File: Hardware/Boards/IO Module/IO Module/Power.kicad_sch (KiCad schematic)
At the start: 1 part, among them J1 USB_C_Receptacle

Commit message: Updated IO Module Schematics
Added Power, USB hub and USB-JTAG circuits
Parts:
- added C1, C16, C17, C21, C22, C23, C27, C7, C8, C9: 10uF, Capacitor_SMD:C_0603_1608Metric, symbol Device:C_Small
- added C10, C11, C12, C13, C25, C26: 22uF, Capacitor_SMD:C_0805_2012Metric, symbol Device:C_Small
- added C14, C18, C2, C24: 100nF, Capacitor_SMD:C_0402_1005Metric, symbol Device:C_Small
- added C15, C28: 1uF, Capacitor_SMD:C_0402_1005Metric, symbol Device:C_Small
- added C19, C20: 100uF, Capacitor_SMD:C_0805_2012Metric, symbol Device:C_Small
- added C3, C4: 10nF, Capacitor_SMD:C_0402_1005Metric, symbol Device:C_Small
- added C5, C6: 330pF, Capacitor_SMD:C_0402_1005Metric, symbol Device:C_Small
- added D1: 1V8 FLT, LED_SMD:LED_0603_1608Metric, symbol Device:LED
- added D2: 3V3 FLT, LED_SMD:LED_0603_1608Metric, symbol Device:LED
- added D3: 3V3 ON, LED_SMD:LED_0603_1608Metric, symbol Device:LED
- added D4: 1V8 ON, LED_SMD:LED_0603_1608Metric, symbol Device:LED
- added Q1: IRLML6244, Package_TO_SOT_SMD:SOT-23, symbol Transistor_FET:IRLML6244
- added R1, R14, R15, R16, R2, R24, R26: 3.3K, Resistor_SMD:R_0402_1005Metric, symbol Device:R_US
- added R10: 162K, Resistor_SMD:R_0402_1005Metric, symbol Device:R_US
- added R11: 38K, Resistor_SMD:R_0402_1005Metric, symbol Device:R_US
- added R12: 190K, Resistor_SMD:R_0402_1005Metric, symbol Device:R_US
- added R13: 9.5K, Resistor_SMD:R_0402_1005Metric, symbol Device:R_US
- added R17, R18, R19, R20: 33R, Resistor_SMD:R_0402_1005Metric, symbol Device:R_US
- added R21: 8.06K, Resistor_SMD:R_0402_1005Metric, symbol Device:R_US
- added R22, R28, R3, R4, R5: 10K, Resistor_SMD:R_0402_1005Metric, symbol Device:R_US
- added R23: 26.7K, Resistor_SMD:R_0402_1005Metric, symbol Device:R_US
- added R25: 23.2K, Resistor_SMD:R_0402_1005Metric, symbol Device:R_US
- added R27: 19.8K, Resistor_SMD:R_0402_1005Metric, symbol Device:R_US
- added R29, R30, R31: 1K, Resistor_SMD:R_0402_1005Metric, symbol Device:R_US
- added R6: 198.2K, Resistor_SMD:R_0402_1005Metric, symbol Device:R_US
- added R7: 2.28K, Resistor_SMD:R_0402_1005Metric, symbol Device:R_US
- added R8: 9.4K, Resistor_SMD:R_0402_1005Metric, symbol Device:R_US
- added R9: 191K, Resistor_SMD:R_0402_1005Metric, symbol Device:R_US
- added U1: TPS25730D, IO_Module:TPS25730DREFR, symbol IO_Module:TPS25730D
- added U10: TPD2EUSB30A, Package_TO_SOT_SMD:Texas_DRT-3, symbol Power_Protection:TPD2EUSB30A
- added U11, U9: TPD4EUSB30, Package_SON:USON-10_2.5x1.0mm_P0.5mm, symbol Power_Protection:TPD4EUSB30
- added U2: INA700AYWFR, IO_Module:INA700_AYWFR, symbol IO_Module:INA700
- added U3, U4: TPSM33625RDNR, IO_Module:RDN0011A-MFG, symbol IO_Module:TPSM33625
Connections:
- net GND: now also C1.2, C10.2, C11.2, C12.2, C13.2, C14.2, C15.2, C16.2, C17.2, C18.2, C19.2, C2.2, C20.2, C21.2, C22.2, C23.2, C24.2, C25.2, C26.2, C27.2, C28.2, C3.2, C4.2, C5.2, C6.2, C7.2, C8.2, C9.2, D3.1 (K), Q1.2 (S), R11.1, R13.1, R22.1, R23.1, R27.1, R28.1, R3.1, R31.1, R4.1, R5.1, R7.1, R9.1, U1.11 (GND), U1.12 (GND), U1.14 (GND), U1.16 (GND), U1.17 (GND), U1.31 (GND), U1.34 (GND), U1.35 (GND), U1.39 (EPAD_GND), U10.3 (GND), U11.3 (GND), U11.8 (GND), U2.B1 (GND), U2.B2 (A0), U3.10 (GND), U4.10 (GND), U9.3 (GND), U9.8 (GND)
- net USB3_RX2_N: now reaches J1.A10 (RX2-)
- net USB3_RX2_N: now also U11.2 (D1-), U11.9 (NC)
- net USB3_RX2_P: now reaches J1.A11 (RX2+)
- net USB3_RX2_P: now also U11.1 (D1+), U11.10 (NC)
- net USB3_TX1_P: now reaches J1.A2 (TX1+)
- net USB3_TX1_P: now also U9.4 (D2+), U9.7 (NC)
- net USB3_TX1_N: now reaches J1.A3 (TX1-)
- net USB3_TX1_N: now also U9.5 (D2-), U9.6 (NC)
- net VBUS_IN: now reaches J1.A4 (VBUS), J1.A9 (VBUS), J1.B4 (VBUS), J1.B9 (VBUS)
- net VBUS_IN: now also C1.1, C2.1, C3.1, C4.1, U1.23 (VBUS_IN), U1.24 (VBUS_IN), U1.25 (VBUS_IN), U1.32 (VBUS), U1.33 (VBUS)
- net USB_CC1: now reaches J1.A5 (CC1)
- net USB_CC1: now also C5.1, U1.28 (CC1)
- net USB2_D_P: now reaches J1.A6 (D+)
- net USB2_D_P: now also J1.B6 (D+), U10.1 (D+)
- net USB2_D_N: now reaches J1.A7 (D-)
- net USB2_D_N: now also J1.B7 (D-), U10.2 (D-)
- net USB3_RX1_N: now reaches J1.B10 (RX1-)
- net USB3_RX1_N: now also U9.2 (D1-), U9.9 (NC)
- net USB3_RX1_P: now reaches J1.B11 (RX1+)
- net USB3_RX1_P: now also U9.1 (D1+), U9.10 (NC)
- net USB3_TX2_P: now reaches J1.B2 (TX2+)
- net USB3_TX2_P: now also U11.4 (D2+), U11.7 (NC)
- net USB3_TX2_N: now reaches J1.B3 (TX2-)
- net USB3_TX2_N: now also U11.5 (D2-), U11.6 (NC)
- net USB_CC2: now reaches J1.B5 (CC2)
- net USB_CC2: now also C6.1, U1.29 (CC2)
- new net: R4.2, U1.27 (NC)
- new net: D3.2 (A), R29.2
- new net: D1.1 (K), U3.1 (PGOOD)
- new net: R23.2, U3.11 (RT)
- new net: C15.1, U3.8 (VCC)
- new net: C28.1, U4.8 (VCC)
- new net: D2.1 (K), U4.1 (PGOOD)
- new net: D2.2 (A), R26.2
- new net: D4.1 (K), Q1.3 (D)
- new net: D4.2 (A), R30.1
- new net: R5.2, U1.36 (NC)
- new net: R3.2, U1.26 (NC)
- new net: D1.2 (A), R24.2
- new net: R27.2, U4.11 (RT)
- new net +1V8: C19.1, C20.1, C21.1, Q1.1 (G), R21.2, R31.2, U3.4 (VOUT)
- new net +3V3: C14.1, C25.1, C26.1, C27.1, R14.2, R15.2, R16.2, R25.2, R29.1, R30.2, U2.C1 (VS), U4.4 (VOUT)
- new net I2C0_SCL: R14.1, R17.1, R19.2
- new net I2C0_SDA: R15.1, R18.1, R20.2
- new net I2CT_SCL: R19.1, R2.1, U1.9 (I2CT_SCL)
- new net I2CT_SDA: R1.1, R20.1, U1.8 (I2CT_SDA)
- new net LDO_1V5: C9.1, U1.4 (LDO_1V5)
- new net LDO_3V3: C8.1, R1.2, R10.2, R12.2, R2.2, R24.1, R26.1, R6.2, R8.2, U1.1 (LDO_3V3)
- new net PP1V8_FB: R21.1, R22.2, U3.9 (FB)
- new net PP3V3_FB: R25.1, R28.2, U4.9 (FB)
- new net PP_VUSB: U2.A1 (IN-)
- new net PP_VUSB_R: C10.1, C11.1, C12.1, C13.1, C16.1, C17.1, C18.1, C22.1, C23.1, C24.1, U1.20 (PPHV), U1.21 (PPHV), U1.22 (PPHV), U2.A3 (IN+), U3.2 (EN), U3.3 (VIN), U4.2 (EN), U4.3 (VIN)
- new net USBPD_ADCIN1: R6.1, R7.2, U1.2 (ADCIN1)
- new net USBPD_ADCIN2: R8.1, R9.2, U1.3 (ADCIN2)
- new net USBPD_ADCIN3: R10.1, R11.2, U1.5 (ADCIN3)
- new net USBPD_ADCIN4: R12.1, R13.2, U1.7 (ADCIN4)
- new net USBPD_CAP_MIS: U1.6 (CAP_MIS)
- new net USBPD_DBG_ACC: U1.10 (DBG_ACC)
- new net USBPD_DRAIN: U1.15 (DRAIN), U1.30 (DRAIN), U1.40 (EPAD_DRAIN)
- new net USBPD_FLT_IN: U1.18 (~{FAULT_IN})
- new net USBPD_PLG_EVNT: U1.37 (PLUG_EVENT)
- new net USBPD_PLG_FLIP: U1.13 (PLUG_FLIP)
- new net USBPD_SINK_EN: U1.19 (~{SINK_EN})
- new net VIN_3V3: C7.1, U1.38 (VIN_3V3)
- new net VUSB_ISNS_ALRT: R16.1, U2.C2 (ALRT)
- new net VUSB_ISNS_SCL: R17.2, U2.C3 (SCL)
- new net VUSB_ISNS_SDA: R18.2, U2.B3 (SDA)
- no-connect marks 0 -> 8
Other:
- note added: "1V8 DCDC"
- note added: "3V3 DCDC"
- note added: "ESD DIODES"
- note added: "OUTPUT PORTS"
- note added: "PWR IN + USB-PD CONTROLLER"
- moved on the sheet: J1

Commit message: Completed IO Module Schematics
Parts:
- J1: footprint (none) -> Connector_USB:USB_C_Receptacle_Amphenol_12401548E4-2A
- renumbered C5 to C10, C6 to C11, C7 to C12, C8 to C13, C9 to C14, C22 to C15, C23 to C16, C24 to C17, C25 to C18, C26 to C19, C27 to C20, C28 to C21, C16 to C22, C17 to C23, C18 to C24, C19 to C25, C20 to C26, C21 to C27, C15 to C28, C10 to C5, C11 to C6, C12 to C7, C13 to C8, C14 to C9, D2 to D1, D3 to D2, D4 to D3, D1 to D4, R6 to R10, R8 to R11, R7 to R12, R9 to R13, R10 to R14, R12 to R15, R1 to R16, R2 to R17, R11 to R18, R13 to R19, R3 to R20, R4 to R21, R5 to R22, R26 to R23, R29 to R24, R27 to R26, R28 to R27, R30 to R28, R24 to R29, R17 to R3, R21 to R30, R23 to R32, R22 to R33, R15 to R4, R14 to R5, R16 to R6, R18 to R7, R19 to R8, R20 to R9, U4 to U3, U10 to U4, U9 to U5, U3 to U6, U11 to U7

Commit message: PCB Layout Started
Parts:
- J1: footprint Connector_USB:USB_C_Receptacle_Amphenol_12401548E4-2A -> Connector_USB:USB_C_Receptacle_Amphenol_12401610E4-2A
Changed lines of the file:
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@@
 			)
 		)
-		(property "Footprint" "Connector_USB:USB_C_Receptacle_Amphenol_12401548E4-2A"
+		(property "Footprint" "Connector_USB:USB_C_Receptacle_Amphenol_12401610E4-2A"
 			(at 33.02 49.53 0)
 			(effects

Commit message: Updated SCH with notes & annotations
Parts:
- J1: footprint Connector_USB:USB_C_Receptacle_Amphenol_12401610E4-2A -> IO_Module:GCT_USB4056-03-A_REVA2
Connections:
- net USB3_RX1_N: now also U5.4 (D2+), U5.7 (NC); no longer U5.2 (D1-), U5.9 (NC)
- net USB3_RX1_P: now also U5.5 (D2-), U5.6 (NC); no longer U5.1 (D1+), U5.10 (NC)
- net USB3_TX1_N: now also U5.1 (D1+), U5.10 (NC); no longer U5.5 (D2-), U5.6 (NC)
- net USB3_TX1_P: now also U5.2 (D1-), U5.9 (NC); no longer U5.4 (D2+), U5.7 (NC)

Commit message: Updated PCB routing for IO Module
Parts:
- C10, C11, C17, C2, C21, C24, C28, C3, C4, C9: footprint Capacitor_SMD:C_0402_1005Metric -> Capacitor_SMD:C_0201_0603Metric
- R10, R11, R12, R13, R14, R15, R18, R19, R20, R21, R22, R23, R24, R25, R26, R27, R28, R29, R3, R30, R31, R32, R33, R4, R5, R6, R7, R8, R9: footprint Resistor_SMD:R_0402_1005Metric -> Resistor_SMD:R_0201_0603Metric
- R16, R17: footprint Resistor_SMD:R_0402_1005Metric -> Resistor_SMD:R_0201_0603Metric; now fitted
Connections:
- net USB3_RX1_N: now also J1.B11 (RX1+), U5.5 (D2-), U5.6 (NC); no longer J1.B10 (RX1-), U5.4 (D2+), U5.7 (NC)
- net USB3_RX1_P: now also J1.B10 (RX1-), U5.4 (D2+), U5.7 (NC); no longer J1.B11 (RX1+), U5.5 (D2-), U5.6 (NC)
- net USB3_RX2_N: now also U7.5 (D2-), U7.6 (NC); no longer U7.2 (D1-), U7.9 (NC)
- net USB3_RX2_P: now also U7.4 (D2+), U7.7 (NC); no longer U7.1 (D1+), U7.10 (NC)
- net USB3_TX2_N: now also U7.2 (D1-), U7.9 (NC); no longer U7.5 (D2-), U7.6 (NC)
- net USB3_TX2_P: now also U7.1 (D1+), U7.10 (NC); no longer U7.4 (D2+), U7.7 (NC)

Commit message: Cleaned up routing for IO module
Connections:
- net USB3_TX1_N: now also J1.A2 (TX1+), U5.2 (D1-), U5.9 (NC); no longer J1.A3 (TX1-), U5.1 (D1+), U5.10 (NC)
- net USB3_TX1_P: now also J1.A3 (TX1-), U5.1 (D1+), U5.10 (NC); no longer J1.A2 (TX1+), U5.2 (D1-), U5.9 (NC)
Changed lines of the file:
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@@
 	(wire
 		(pts
-			(xy 226.06 214.63) (xy 212.09 214.63)
-		)
-		(stroke
-			(width 0)
-			(type default)
-		)
-	)
-	(wire
-		(pts
 			(xy 107.95 118.11) (xy 121.92 118.11)
 		)
@@
 	(wire
 		(pts
+			(xy 226.06 224.79) (xy 212.09 224.79)
+		)
+		(stroke
+			(width 0)
+			(type default)
+		)
+	)
+	(wire
+		(pts
 			(xy 106.68 252.73) (xy 120.65 252.73)
 		)
@@
 	(wire
 		(pts
-			(xy 226.06 229.87) (xy 212.09 229.87)
-		)
-		(stroke
-			(width 0)
-			(type default)
-		)
-	)
-	(wire
-		(pts
 			(xy 69.85 83.82) (xy 69.85 82.55)
 		)
@@
 	(wire
 		(pts
+			(xy 226.06 214.63) (xy 212.09 214.63)
+		)
+		(stroke
+			(width 0)
+			(type default)
+		)
+	)
+	(wire
+		(pts
 			(xy 99.06 73.66) (xy 102.87 73.66)
 		)
@@
 	(wire
 		(pts
-			(xy 226.06 224.79) (xy 212.09 224.79)
+			(xy 107.95 130.81) (xy 107.95 132.08)
 		)
 		(stroke
@@
 	(wire
 		(pts
-			(xy 107.95 130.81) (xy 107.95 132.08)
+			(xy 160.02 195.58) (xy 160.02 196.85)
 		)
 		(stroke
@@
 	(wire
 		(pts
-			(xy 160.02 195.58) (xy 160.02 196.85)
+			(xy 119.38 139.7) (xy 119.38 142.24)
 		)
 		(stroke
@@
 	(wire
 		(pts
-			(xy 119.38 139.7) (xy 119.38 142.24)
+			(xy 33.02 114.3) (xy 50.8 114.3)
 		)
 		(stroke
@@
 	(wire
 		(pts
-			(xy 33.02 114.3) (xy 50.8 114.3)
+			(xy 71.12 45.72) (xy 71.12 31.75)
 		)
 		(stroke
@@
 	(wire
 		(pts
-			(xy 71.12 45.72) (xy 71.12 31.75)
+			(xy 226.06 229.87) (xy 212.09 229.87)
 		)
 		(stroke
@@
 	(wire
 		(pts
-			(xy 226.06 219.71) (xy 212.09 219.71)
+			(xy 87.63 45.72) (xy 87.63 48.26)
 		)
 		(stroke
@@
 	(wire
 		(pts
-			(xy 87.63 45.72) (xy 87.63 48.26)
+			(xy 120.65 207.01) (xy 120.65 208.28)
 		)
 		(stroke
@@
 	(wire
 		(pts
-			(xy 120.65 207.01) (xy 120.65 208.28)
+			(xy 226.06 219.71) (xy 212.09 219.71)
 		)
 		(stroke
@@
 		)
 	)
-	(label "USB3_TX1_N"
-		(at 212.09 219.71 0)
-		(fields_autoplaced yes)
-		(effects
-			(font
-				(size 1.27 1.27)
-			)
-			(justify left bottom)
-		)
-	)
 	(label "I2C0_SDA"
 		(at 280.67 36.83 180)
@@
 		)
 	)
-	(label "USB3_TX1_P"
+	(label "USB3_TX1_N"
+		(at 58.42 59.69 180)
+		(fields_autoplaced yes)
+		(effects
+			(font
+				(size 1.27 1.27)
+			)
+			(justify right bottom)
+		)
+	)
+	(label "USB3_TX1_N"
 		(at 212.09 229.87 0)
 		(fields_autoplaced yes)
@@
 		)
 	)
+	(label "USB3_TX1_P"
+		(at 212.09 214.63 0)
+		(fields_autoplaced yes)
+		(effects
+			(font
+				(size 1.27 1.27)
+			)
+			(justify left bottom)
+		)
+	)
 	(label "USB3_RX1_N"
 		(at 58.42 52.07 180)
@@
 		)
 	)
-	(label "USB3_TX1_N"
+	(label "USB3_TX1_P"
 		(at 58.42 57.15 180)
 		(fields_autoplaced yes)
@@
 		)
 	)
-	(label "USB3_TX1_N"
-		(at 212.09 214.63 0)
-		(fields_autoplaced yes)
-		(effects
-			(font
-				(size 1.27 1.27)
-			)
-			(justify left bottom)
-		)
-	)
-	(label "USB3_TX1_P"
-		(at 58.42 59.69 180)
-		(fields_autoplaced yes)
-		(effects
-			(font
-				(size 1.27 1.27)
-			)
-			(justify right bottom)
-		)
-	)
 	(label "LDO_3V3"
 		(at 207.01 73.66 0)
@@
 		)
 	)
+	(label "USB3_TX1_N"
+		(at 212.09 224.79 0)
+		(fields_autoplaced yes)
+		(effects
+			(font
+				(size 1.27 1.27)
+			)
+			(justify left bottom)
+		)
+	)
 	(label "USB3_TX2_P"
 		(at 58.42 74.93 180)
@@
 		)
 	)
-	(label "USB3_TX1_P"
-		(at 212.09 224.79 0)
-		(fields_autoplaced yes)
-		(effects
-			(font
-				(size 1.27 1.27)
-			)
-			(justify left bottom)
-		)
-	)
 	(label "I2C0_SDA"
 		(at 388.62 39.37 180)
@@
 		(fields_autoplaced yes)
 		(effects
+			(font
+				(size 1.27 1.27)
+			)
+			(justify left bottom)
+		)
+	)
+	(label "USB3_TX1_P"
+		(at 212.09 219.71 0)
+		(fields_autoplaced yes)
+		(effects

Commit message: Using new DP to HDMI IC
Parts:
- removed U5, U7: TPD4EUSB30, Package_SON:USON-10_2.5x1.0mm_P0.5mm, symbol Power_Protection:TPD4EUSB30
- added U17, U26: TPD4E02B04DQA, Package_SON:USON-10_2.5x1.0mm_P0.5mm, symbol Power_Protection:TPD4E02B04DQA
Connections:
- net GND: now also U17.3 (G), U17.8 (G), U26.3 (G), U26.8 (G)
- net USB3_RX1_N: now also U17.5 (IO4), U17.6 (NC)
- net USB3_RX1_P: now also U17.4 (IO3), U17.7 (NC)
- net USB3_RX2_N: now also U26.5 (IO4), U26.6 (NC)
- net USB3_RX2_P: now also U26.4 (IO3), U26.7 (NC)
- net USB3_TX1_N: now also U17.2 (IO2), U17.9 (NC)
- net USB3_TX1_P: now also U17.1 (IO1), U17.10 (NC)
- net USB3_TX2_N: now also U26.2 (IO2), U26.9 (NC)
- net USB3_TX2_P: now also U26.1 (IO1), U26.10 (NC)

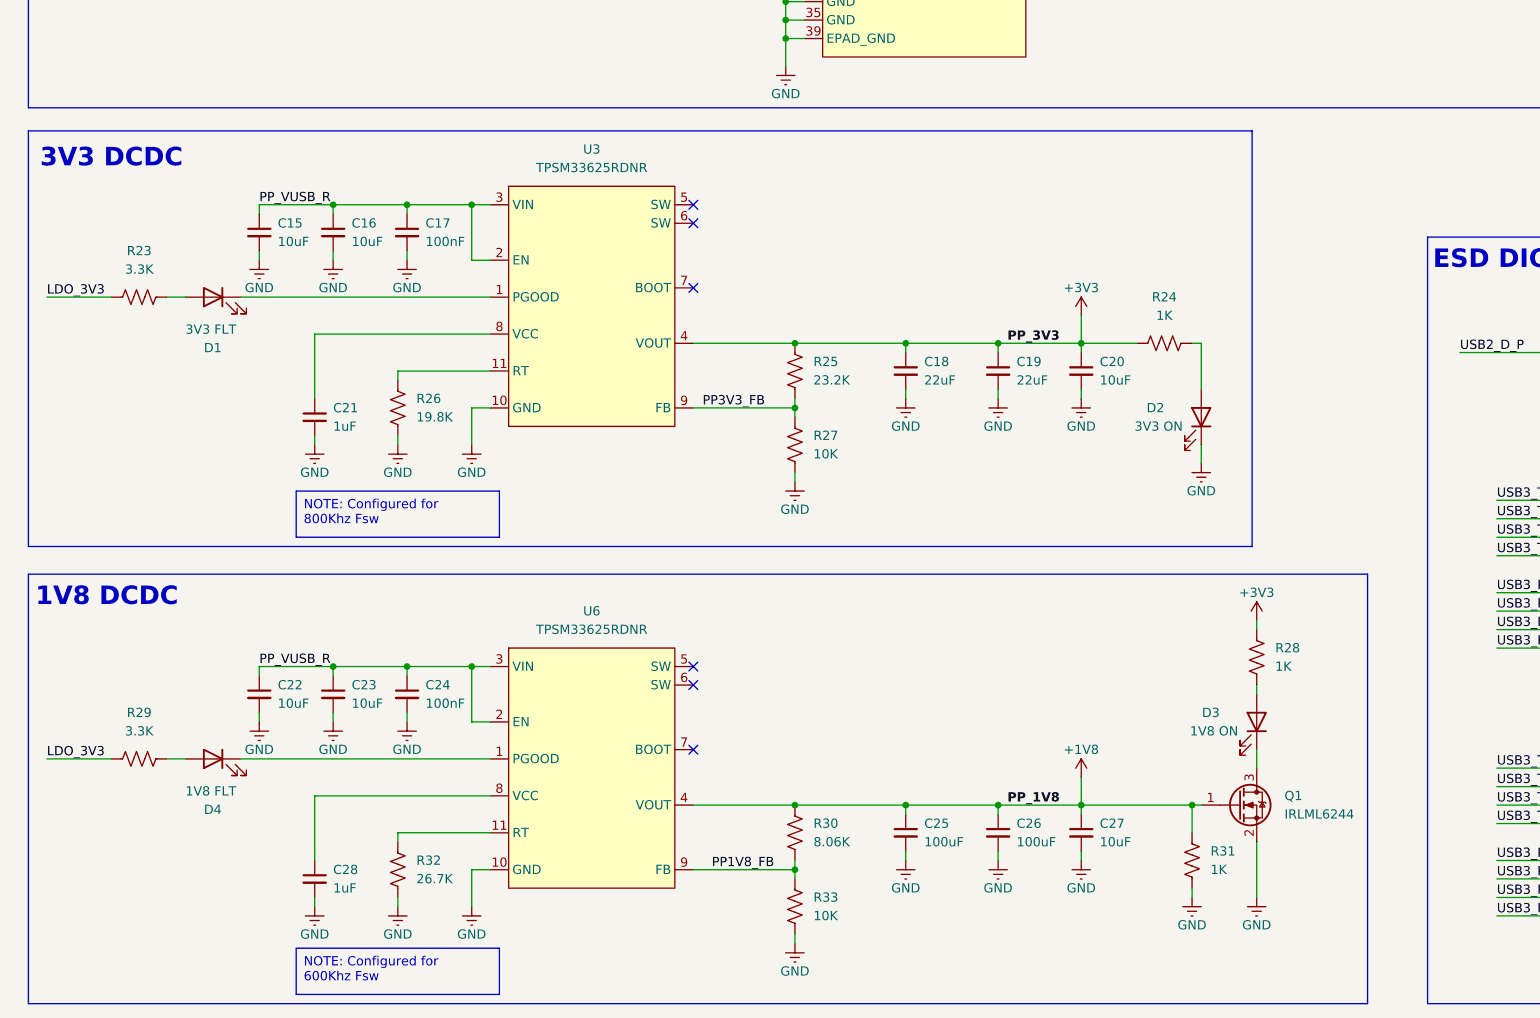
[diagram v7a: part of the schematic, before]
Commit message: Cleaned up IO Module and went through DRC errors
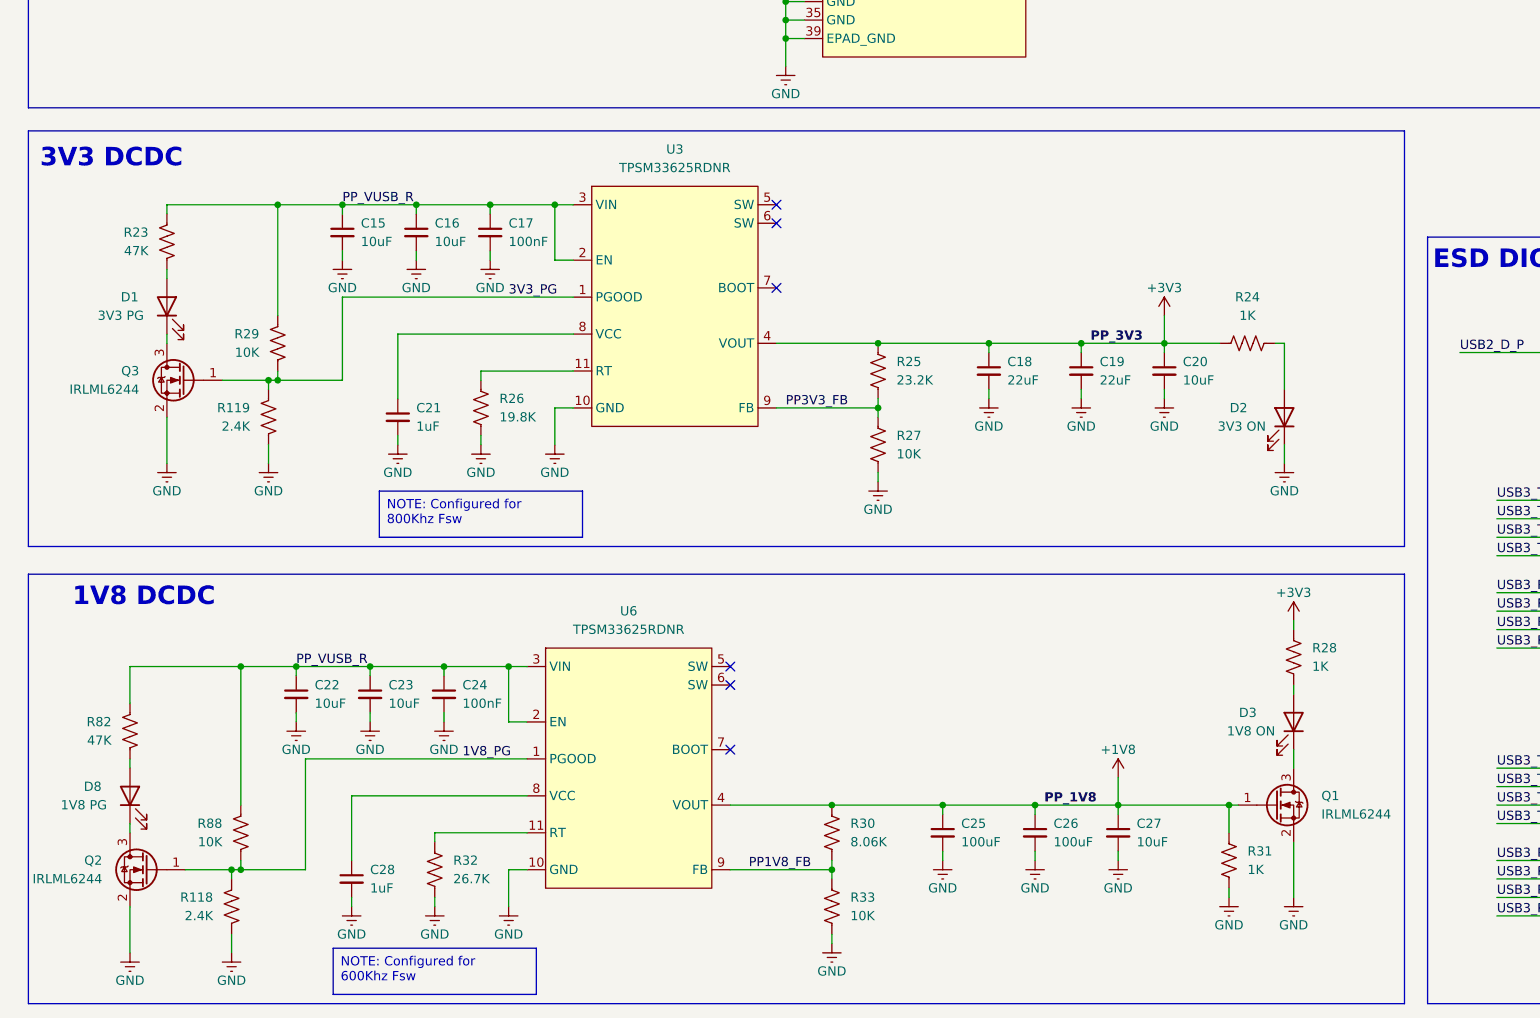
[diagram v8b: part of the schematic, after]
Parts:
- removed D4: 1V8 FLT, LED_SMD:LED_0603_1608Metric, symbol Device:LED
- added D8: 1V8 PG, LED_SMD:LED_0603_1608Metric, symbol Device:LED
- added Q2, Q3: IRLML6244, Package_TO_SOT_SMD:SOT-23, symbol Transistor_FET:IRLML6244
- added R118, R119: 2.4K, Resistor_SMD:R_0402_1005Metric, symbol Device:R_US
- added R82: 47K, Resistor_SMD:R_0402_1005Metric, symbol Device:R_US
- added R88: 10K, Resistor_SMD:R_0402_1005Metric, symbol Device:R_US
- D1: value 3V3 FLT -> 3V3 PG
- R23: value 3.3K -> 47K; footprint Resistor_SMD:R_0201_0603Metric -> Resistor_SMD:R_0402_1005Metric
- R29: value 3.3K -> 10K; footprint Resistor_SMD:R_0201_0603Metric -> Resistor_SMD:R_0402_1005Metric
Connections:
- net GND: now also Q2.2 (S), Q3.2 (S), R118.1, R119.1
- net LDO_3V3: no longer R23.1, R29.1
- net PP_VUSB_R: now also R23.2, R29.2, R82.2, R88.2
- net 1V8_PG: now reaches U6.1 (PGOOD)
- net 1V8_PG: now also Q2.1 (G), R118.2, R88.1
- net at D1.1 (K): now also Q3.3 (D); no longer U3.1 (PGOOD)
- net at D1.2 (A): now also R23.1; no longer R23.2
- new net: D8.1 (K), Q2.3 (D)
- new net: D8.2 (A), R82.1
- new net 3V3_PG: Q3.1 (G), R119.2, R29.1, U3.1 (PGOOD)
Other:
- moved on the sheet: C15, C16, C17, C18, C19, C20, C21, C22, C23, C24, C25, C26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
